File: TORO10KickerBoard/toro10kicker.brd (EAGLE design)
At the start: 100 x 40 mm, 94 parts, among them CN2 43650-0800, CN3 ARM-JTAG, CN4 5569-04A2, CN5 5569-02A2, CN6 5569-02A2, Q1 BSS138, Q2 BSS138, Q3 CSD19538Q3A, Q4 BSS138, U1 NJM7812S, U2 NJM7805S, U3 SAMC21E18A-A, U4 LT3751EUFD, U5 INA181A1IDBV, U6 UCC27524DGN

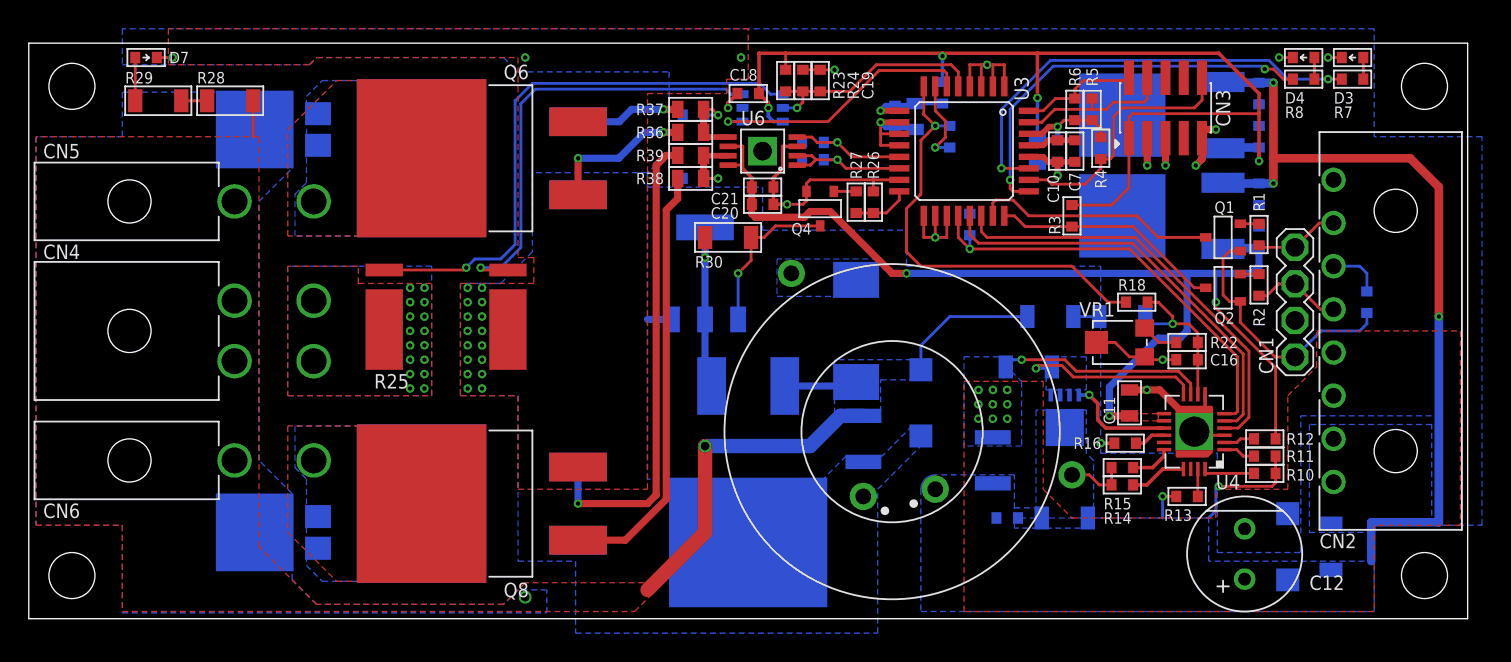
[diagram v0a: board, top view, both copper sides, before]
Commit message: add kicker BOM
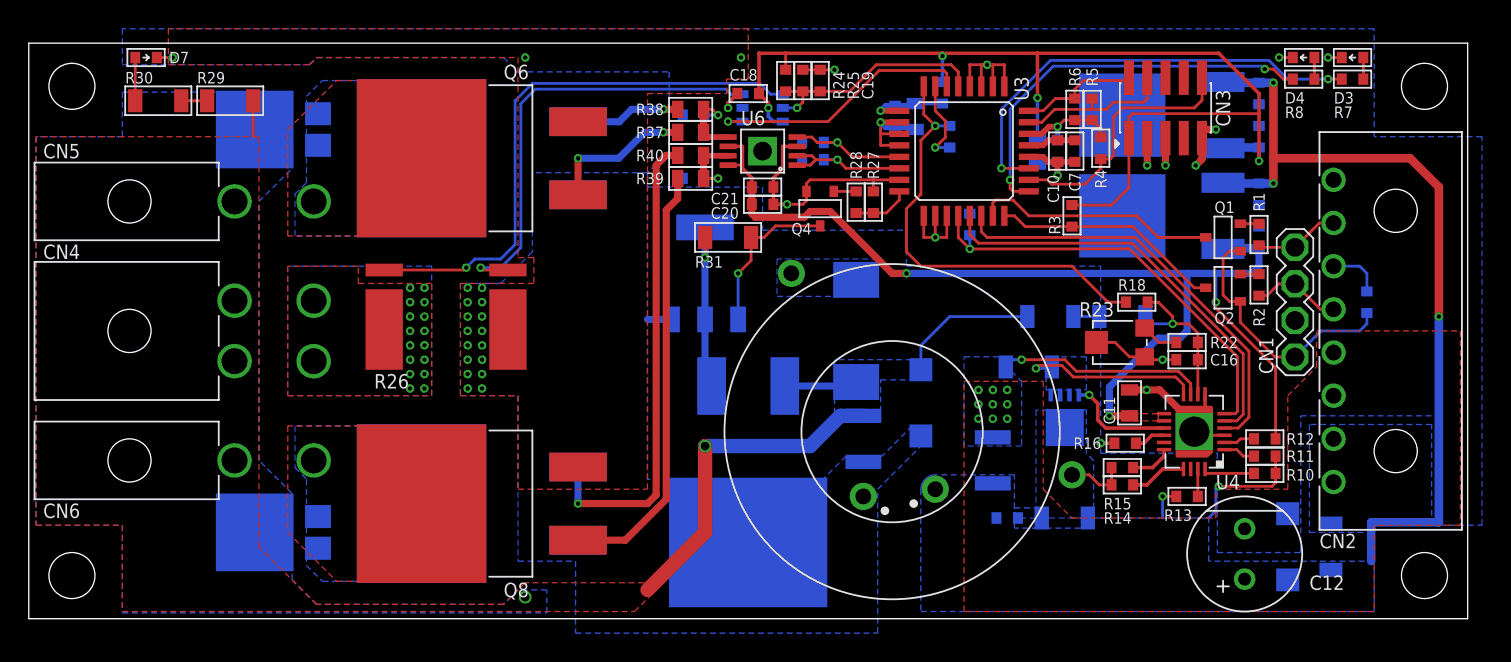
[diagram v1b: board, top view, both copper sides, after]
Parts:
- removed VR1: TC33X-2-501E, kiks-passive:TC33X
- added R40: 10, kiks-passive:2012
- D3: value (none) -> Green
- D4: value (none) -> Orange
- FB1: value BLM18PG471 -> BLM18PG471SN1D
- Q5: value (none) -> BSP130
- R23: value 10k -> TC33X-2-501E; device kiks-passive:1608 -> kiks-passive:TC33X
- R25: value WSL4026L3000FEB -> 10k; device kiks-passive:WSL4026 -> kiks-passive:1608
- R26: value 10k -> WSL4026L3000FEB; device kiks-passive:1608 -> kiks-passive:WSL4026
- R27: value 1k -> 10k
- R28: value 100k -> 1k; device kiks-passive:3216 -> kiks-passive:1608
- R30: value 1M -> 100k
- R31: value PFS35-1KF1 -> 1M; device kiks-passive:D2PAK-3 -> kiks-passive:3216
- R32: value 4.7k -> PFS35-1KF1; device kiks-passive:1608 -> kiks-passive:D2PAK-3
- R34: value DNC -> 4.7k
- R36: value 10 -> DNC; device kiks-passive:2012 -> kiks-passive:1608
- moved R28 44.1 mm to (57.5, 28.9), turned to 90 degrees
- moved R30 40.7 mm to (9.00, 36.0), turned to 0 degrees
- moved R26 30.7 mm to (29.0, 21.0), turned to 180 degrees
- moved R25 29.7 mm to (53.8, 37.4), turned to 270 degrees
- moved R23 29.4 mm to (75.7, 19.2)
- moved R32 19.4 mm to (50.0, 13.0)
- moved R31 13.6 mm to (48.6, 26.5), flipped to the top
- moved R34 8.51 mm to (54.5, 33.1)
- moved R29 5.00 mm to (14.0, 36.0)
- moved R38 4.80 mm to (46.0, 35.4)
- moved R35 4.40 mm to (46.2, 35.0)
- moved R36 3.21 mm to (46.2, 30.6), flipped to the bottom
- moved R37 1.60 mm to (46.0, 33.8)
- moved R39 1.60 mm to (46.0, 30.6)
- moved R27 1.20 mm to (58.7, 28.9), turned to 270 degrees
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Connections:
- net !CAP_DISCHARGE: now also R27.2, R28.1; no longer R26.2, R27.1
- net +5V: now also R24.2; no longer R23.2
- net CAP_CURRENT_BIAS: now also R24.1, R25.2; no longer R23.1, R24.2
- net GND: now also R23.1, R23.2, R25.1, R26.1A, R27.1, R32.4, R36.1; no longer R24.1, R25.1A, R26.1, R31.4, R32.1, VR1.1, VR1.2
- net KICKER_KICK1: now also R33.2; no longer R32.2
- net KICKER_KICK2: now also R34.2; no longer R33.2
- net N$14: now also R23.3; no longer VR1.3
- net N$19: now also R26.2A; no longer R25.2A
- net N$21: now also R29.1, R30.2; no longer R28.1, R29.2
- net N$23: now also R37.2; no longer R36.2
- net N$24: now also R38.2; no longer R37.2
- net N$25: now also R35.2, R38.1; no longer R34.2, R36.1
- net N$26: now also R39.2; no longer R38.2
- net N$27: now also R40.2; no longer R39.2
- net N$28: now also R36.2, R40.1; no longer R35.2, R38.1
- net N$30: now also R31.1; no longer R30.1
- net N$32: now also R28.2; no longer R27.2
- net N$33: now also R30.1; no longer R29.1
- net N$36: now also R26.2B; no longer R25.2B
- net N$37: now also R26.1B; no longer R25.1B
- net N$8: now also R31.2, R32.1; no longer R30.2, R31.1
- net VCAP: now also R29.2, R32.3; no longer R28.2, R31.3
